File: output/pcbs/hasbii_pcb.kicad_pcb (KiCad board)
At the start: 2 copper layers, 160.9 x 104.5 mm, 58 parts

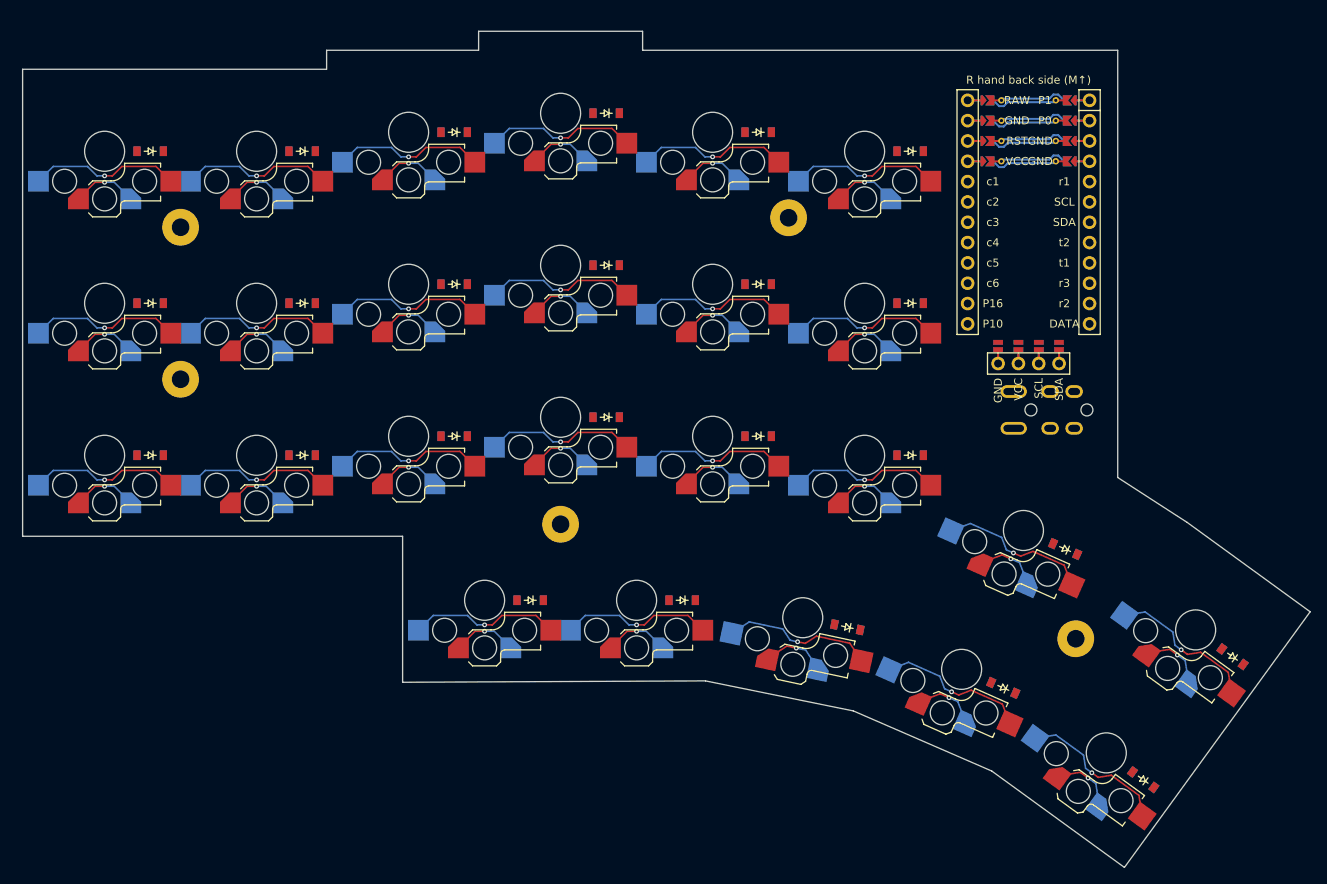
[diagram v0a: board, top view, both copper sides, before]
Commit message: refactor: overhaul layout config with column renaming, new units, and reset switch zone
- Reverse column order so c1=inner, c6=outer pinky (more intuitive left-to-right)
- Adjust stagger from u/8 to u/6 for more pronounced finger stagger
- Rename thumbfan rows t1/t2 → r4/r5 for consistent naming across zones
- Reorder thumbfan columns (c3/c4/c5/c6) and update anchor ref to matrix_c3_r3
- Remove display zone from points; remove `a` unit variable
- Add spacing, trrsw, trrsh, reset_switch_size unit variables; round mcuw to 18
- Reposition MCU anchor to matrix_c6_r1 with spacing-based offset
- Reposition TRRS jack below MCU; add reset_switch zone below TRRS
- Update screw hole aggregate refs to reflect new column names
- Bump engine version to 4.2.1; regenerate DXF outlines and KiCad PCB

Co-Authored-By: Claude Sonnet 4.6 <noreply@anthropic.com>
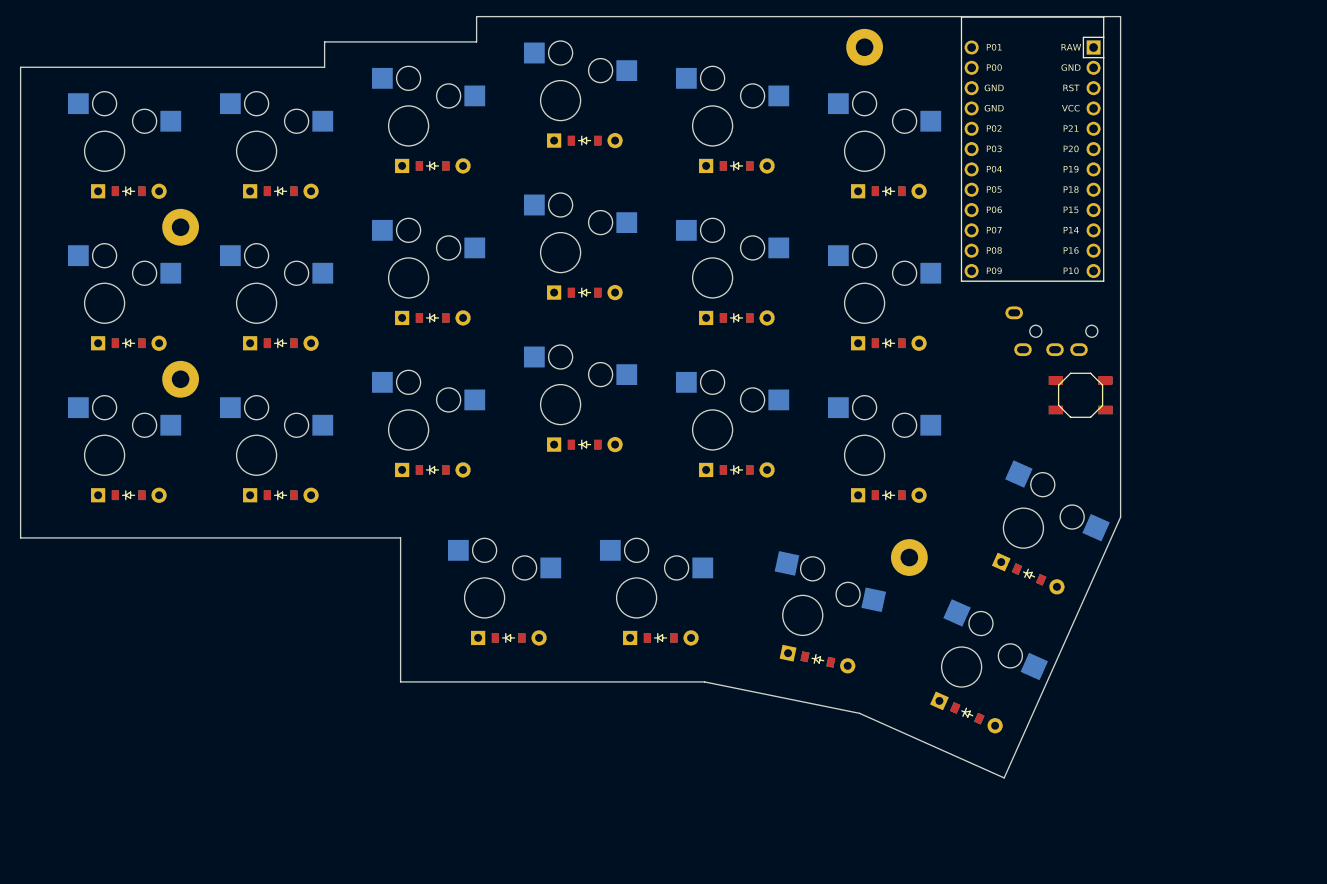
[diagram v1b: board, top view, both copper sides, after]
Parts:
- removed D24, D25: , ceoloide:diode_tht_sod123
- removed DISP1: , ceoloide:display_ssd1306
- removed MH5: , ceoloide:mounting_hole_npth
- removed S24, S25: , ceoloide:switch_choc_v1_v2
- added B1: , E73:SW_TACT_ALPS_SKQGABE010, F.Cu at (272.0, 142.5)
- D1, D10, D11, D12, D13, D14, D15, D16, D17, D18, D19, D2, D20, D21, D22, D23, D3, D4, D5, D6, D7, D8, D9: footprint ceoloide:diode_tht_sod123 -> ComboDiode
- MCU1: footprint ceoloide:mcu_supermini_nrf52840 -> ProMicro
- TRRS1: footprint ceoloide:trrs_pj320a (reversible, symmetric) -> ceoloide:trrs_pj320a
- moved MH4 100.0 mm to (250.6, 162.8), turned to -18 degrees
- moved MH3 78.5 mm to (245.0, 99.0), turned to 0 degrees
- moved MH1 76.0 mm to (159.5, 121.5)
- moved MH2 50.8 mm to (159.5, 140.5)
- moved TRRS1 9.85 mm to (275.0, 134.5)
- moved D1 5.68 mm to (153.0, 155.0), turned to 0 degrees
- moved D16 5.68 mm to (248.0, 155.0), turned to 0 degrees
- moved D17 5.68 mm to (248.0, 136.0), turned to 0 degrees
- moved D18 5.68 mm to (248.0, 117.0), turned to 0 degrees
- moved D2 5.68 mm to (153.0, 136.0), turned to 0 degrees
- moved D3 5.68 mm to (153.0, 117.0), turned to 0 degrees
- moved D4 5.68 mm to (172.0, 155.0), turned to 0 degrees
- moved D5 5.68 mm to (172.0, 136.0), turned to 0 degrees
- moved D6 5.68 mm to (172.0, 117.0), turned to 0 degrees
- moved D22 5.51 mm to (257.8, 182.3), turned to -24 degrees
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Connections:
- D1 pad 2: c6_r3 -> c1_r3
- D10 pad 2: c3_r3 -> c4_r3
- D11 pad 2: c3_r2 -> c4_r2
- D12 pad 2: c3_r1 -> c4_r1
- D13 pad 2: c2_r3 -> c5_r3
- D14 pad 2: c2_r2 -> c5_r2
- D15 pad 2: c2_r1 -> c5_r1
- D16 pad 2: c1_r3 -> c6_r3
- D17 pad 2: c1_r2 -> c6_r2
- D18 pad 2: c1_r1 -> c6_r1
- D19 pad 1: t2 -> r5
- D19 pad 2: c5_t2 -> c3_r5
- D2 pad 2: c6_r2 -> c1_r2
- D20 pad 1: t2 -> r5
- D20 pad 2: c4_t2 -> c4_r5
- D21 pad 1: t2 -> r5
- D21 pad 2: c3_t2 -> c5_r5
- D22 pad 1: t2 -> r5
- D22 pad 2: c2_t2 -> c6_r5
- D23 pad 1: t1 -> r4
- D23 pad 2: c2_t1 -> c6_r4
- D3 pad 2: c6_r1 -> c1_r1
- D4 pad 2: c5_r3 -> c2_r3
- D5 pad 2: c5_r2 -> c2_r2
- D6 pad 2: c5_r1 -> c2_r1
- D7 pad 2: c4_r3 -> c3_r3
- D8 pad 2: c4_r2 -> c3_r2
- D9 pad 2: c4_r1 -> c3_r1
- MCU1 pad 1: MCU1_1 -> RAW
- MCU1 pad 10: r3 -> P14
- MCU1 pad 11: r2 -> P16
- MCU1 pad 13: P10 -> P1
- MCU1 pad 14: P16 -> P0
- MCU1 pad 15: c6 -> GND
- MCU1 pad 16: c5 -> GND
- MCU1 pad 17: c4 -> P2
- MCU1 pad 18: c3 -> P3
- MCU1 pad 19: c2 -> r1
- MCU1 pad 2: MCU1_2 -> GND
- MCU1 pad 20: c1 -> r2
- MCU1 pad 21: MCU1_21 -> r3
- MCU1 pad 22: MCU1_22 -> r4
- MCU1 pad 23: MCU1_23 -> r5
- MCU1 pad 24: MCU1_24 -> c1
- MCU1 pad 3: MCU1_3 -> RST
- MCU1 pad 4: MCU1_4 -> VCC
- MCU1 pad 5: r1 -> c2
- MCU1 pad 6: SCL -> c3
- MCU1 pad 7: SDA -> c4
- MCU1 pad 8: t2 -> c5
- MCU1 pad 9: t1 -> c6
- S1 pad 1: c6_r3 -> c1
- S1 pad 2: c6 -> c1_r3
- S10 pad 1: c3_r3 -> c4
- S10 pad 2: c3 -> c4_r3
- S11 pad 1: c3_r2 -> c4
- S11 pad 2: c3 -> c4_r2
- S12 pad 1: c3_r1 -> c4
- S12 pad 2: c3 -> c4_r1
- S13 pad 1: c2_r3 -> c5
- S13 pad 2: c2 -> c5_r3
- S14 pad 1: c2_r2 -> c5
- S14 pad 2: c2 -> c5_r2
- S15 pad 1: c2_r1 -> c5
- S15 pad 2: c2 -> c5_r1
- S16 pad 1: c1_r3 -> c6
- S16 pad 2: c1 -> c6_r3
- S17 pad 1: c1_r2 -> c6
- S17 pad 2: c1 -> c6_r2
- S18 pad 1: c1_r1 -> c6
- S18 pad 2: c1 -> c6_r1
- S19 pad 1: c5_t2 -> c3
- S19 pad 2: c5 -> c3_r5
- S2 pad 1: c6_r2 -> c1
- S2 pad 2: c6 -> c1_r2
- S20 pad 1: c4_t2 -> c4
- S20 pad 2: c4 -> c4_r5
- S21 pad 1: c3_t2 -> c5
- S21 pad 2: c3 -> c5_r5
- S22 pad 1: c2_t2 -> c6
- S22 pad 2: c2 -> c6_r5
- S23 pad 1: c2_t1 -> c6
- S23 pad 2: c2 -> c6_r4
- S3 pad 1: c6_r1 -> c1
- S3 pad 2: c6 -> c1_r1
- S4 pad 1: c5_r3 -> c2
- S4 pad 2: c5 -> c2_r3
- S5 pad 1: c5_r2 -> c2
- S5 pad 2: c5 -> c2_r2
- S6 pad 1: c5_r1 -> c2
- S6 pad 2: c5 -> c2_r1
- S7 pad 1: c4_r3 -> c3
- S7 pad 2: c4 -> c3_r3
- S8 pad 1: c4_r2 -> c3
- S8 pad 2: c4 -> c3_r2
- S9 pad 1: c4_r1 -> c3
- S9 pad 2: c4 -> c3_r1
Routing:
- net (no net): track 112.6 -> 0.00 mm
- net c1: track 95.3 -> 0.00 mm, vias 5 -> 0
- net c2: track 95.3 -> 0.00 mm, vias 5 -> 0
- net c3: track 76.3 -> 0.00 mm, vias 4 -> 0
- net c5: track 76.3 -> 0.00 mm, vias 4 -> 0
- net c4: track 76.3 -> 0.00 mm, vias 4 -> 0
- net c6: track 57.2 -> 0.00 mm, vias 3 -> 0
- net c2_t2: track 8.27 -> 0.00 mm, vias 1 -> 0
- net c2_t1: track 8.27 -> 0.00 mm, vias 1 -> 0
- net c6_r1: track 8.27 -> 0.00 mm, vias 1 -> 0
- net c5_r1: track 8.27 -> 0.00 mm, vias 1 -> 0
- net c4_r1: track 8.27 -> 0.00 mm, vias 1 -> 0
- net c3_r1: track 8.27 -> 0.00 mm, vias 1 -> 0
- net c2_r1: track 8.27 -> 0.00 mm, vias 1 -> 0
- net c1_r1: track 8.27 -> 0.00 mm, vias 1 -> 0
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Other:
- board size 160.9 x 104.5 mm -> 137.5 x 95.2 mm

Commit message: feat: wire MCU GP pins and migrate to RP2040 Zero
- Assign all matrix nets to RP2040 Zero GP pins (col2row, GP14-29 for
  columns, GP4/7/8/12/13 for rows, GP9 for TRRS DATA)
- Switch MCU footprint from promicro to rp2040zero; add footprint file
- Fix stagger values (u/8), thumbfan anchor, TRRS params, screw holes
- Remove stale left.kicad_pcb and gerbers_left artifacts
- Update CLAUDE.md: correct column order, units, thumbfan description,
  add GP pin table, change firmware target ZMK → QMK

Co-Authored-By: Claude Sonnet 4.6 <noreply@anthropic.com>
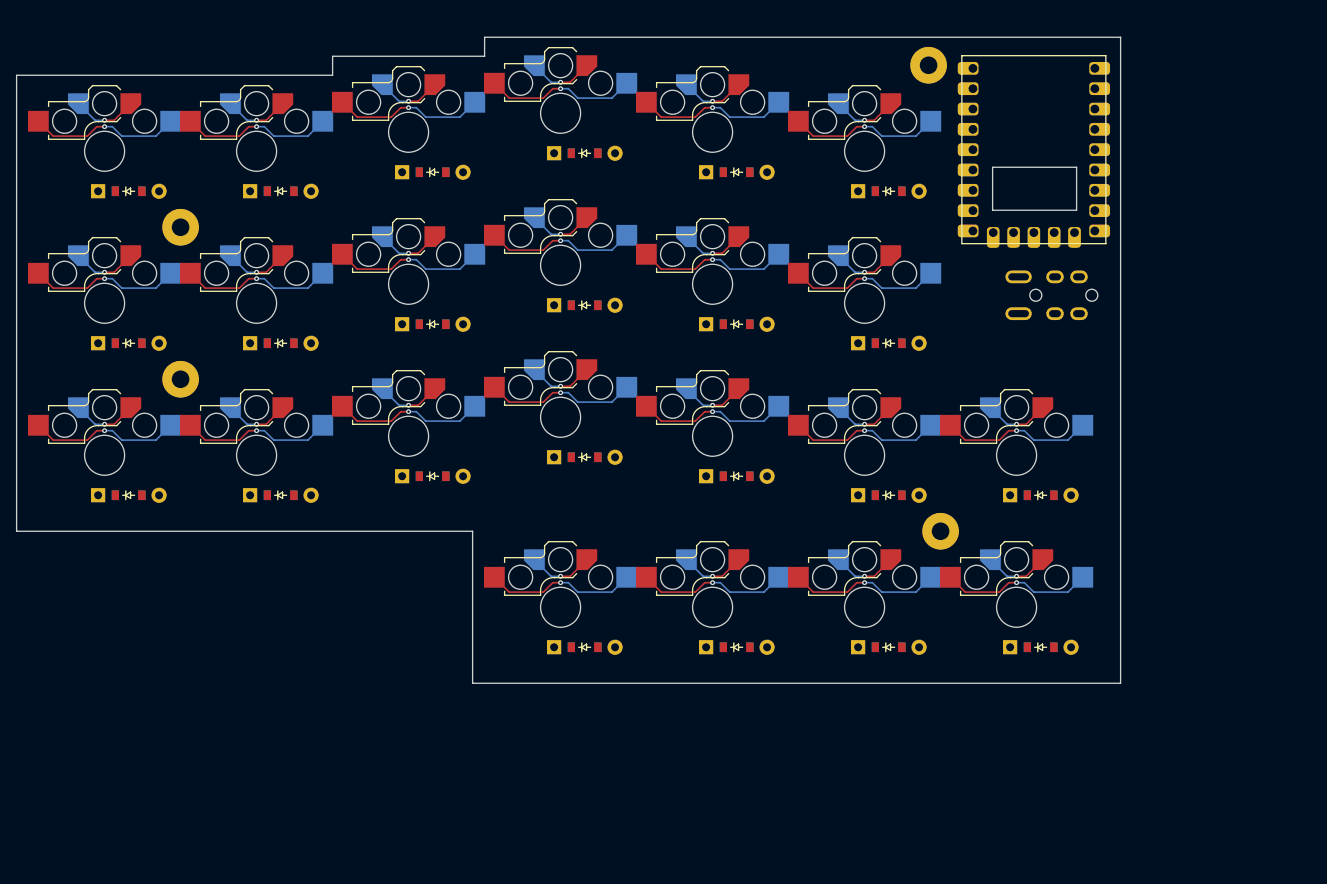
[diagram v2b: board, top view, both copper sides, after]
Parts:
- removed B1: , E73:SW_TACT_ALPS_SKQGABE010
- removed MCU1: , ProMicro
- added RP2040Zero1: , RP2040-Zero, F.Cu at (256.0, 124.5)
- TRRS1: footprint ceoloide:trrs_pj320a -> ceoloide:trrs_pj320a (reversible, symmetric)
- moved D22 12.3 mm to (267.0, 174.0), turned to 0 degrees
- moved S22 10.1 mm to (264.0, 169.0), turned to 0 degrees
- moved D23 10.0 mm to (267.0, 155.0), turned to 0 degrees
- moved D19 9.57 mm to (210.0, 174.0)
- moved D20 9.57 mm to (229.0, 174.0)
- moved S19 9.57 mm to (207.0, 169.0)
- moved S20 9.57 mm to (226.0, 169.0)
- moved S23 9.15 mm to (264.0, 150.0), turned to 0 degrees
- moved D21 8.97 mm to (248.0, 174.0), turned to 0 degrees
- moved MH3 8.31 mm to (253.0, 101.2)
- moved S21 7.80 mm to (245.0, 169.0), turned to 0 degrees
- moved MH4 5.10 mm to (254.5, 159.5), turned to 0 degrees
- moved TRRS1 4.50 mm to (275.0, 130.0)
- moved D10 1.58 mm to (210.0, 150.2)
- moved D11 1.58 mm to (210.0, 131.2)
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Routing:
- net c6: track 0.00 -> 41.3 mm, vias 0 -> 5
- net c5: track 0.00 -> 33.1 mm, vias 0 -> 4
- net c4: track 0.00 -> 33.1 mm, vias 0 -> 4
- net c3: track 0.00 -> 33.1 mm, vias 0 -> 4
- net c2: track 0.00 -> 24.8 mm, vias 0 -> 3
- net c1: track 0.00 -> 24.8 mm, vias 0 -> 3
- net c6_r2: track 0.00 -> 19.1 mm, vias 0 -> 1
- net c2_r2: track 0.00 -> 19.1 mm, vias 0 -> 1
- net c1_r2: track 0.00 -> 19.1 mm, vias 0 -> 1
- net c6_r3: track 0.00 -> 19.1 mm, vias 0 -> 1
- net c5_r5: track 0.00 -> 19.1 mm, vias 0 -> 1
- net c5_r3: track 0.00 -> 19.1 mm, vias 0 -> 1
- net c4_r5: track 0.00 -> 19.1 mm, vias 0 -> 1
- net c4_r3: track 0.00 -> 19.1 mm, vias 0 -> 1
- net c3_r5: track 0.00 -> 19.1 mm, vias 0 -> 1
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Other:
- board size 137.5 x 95.2 mm -> 138 x 80.8 mm
